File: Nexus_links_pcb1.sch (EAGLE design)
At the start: 41 parts, among them IC1 TL074D, IC4 TL074D, J1 PJ301_THONKICONN6, J10 PJ301_THONKICONN6, J11 PJ301_THONKICONN6, J12 PJ301_THONKICONN6, J2 PJ301_THONKICONN6, J3 PJ301_THONKICONN6, J4 PJ301_THONKICONN6, J5 PJ301_THONKICONN6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

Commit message: updated in december
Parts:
- C1, C2: value 4.7u -> 10u; RSPARTNUMBER (none) -> 568-711
- C3: RSPARTNUMBER (none) -> 264-4416
- C9: RSPARTNUMBER (none) -> 601-0198
- D1, D2: RSPARTNUMBER (none) -> 708-2197
- LED1, LED3: RSPARTNUMBER (none) -> 228-5663

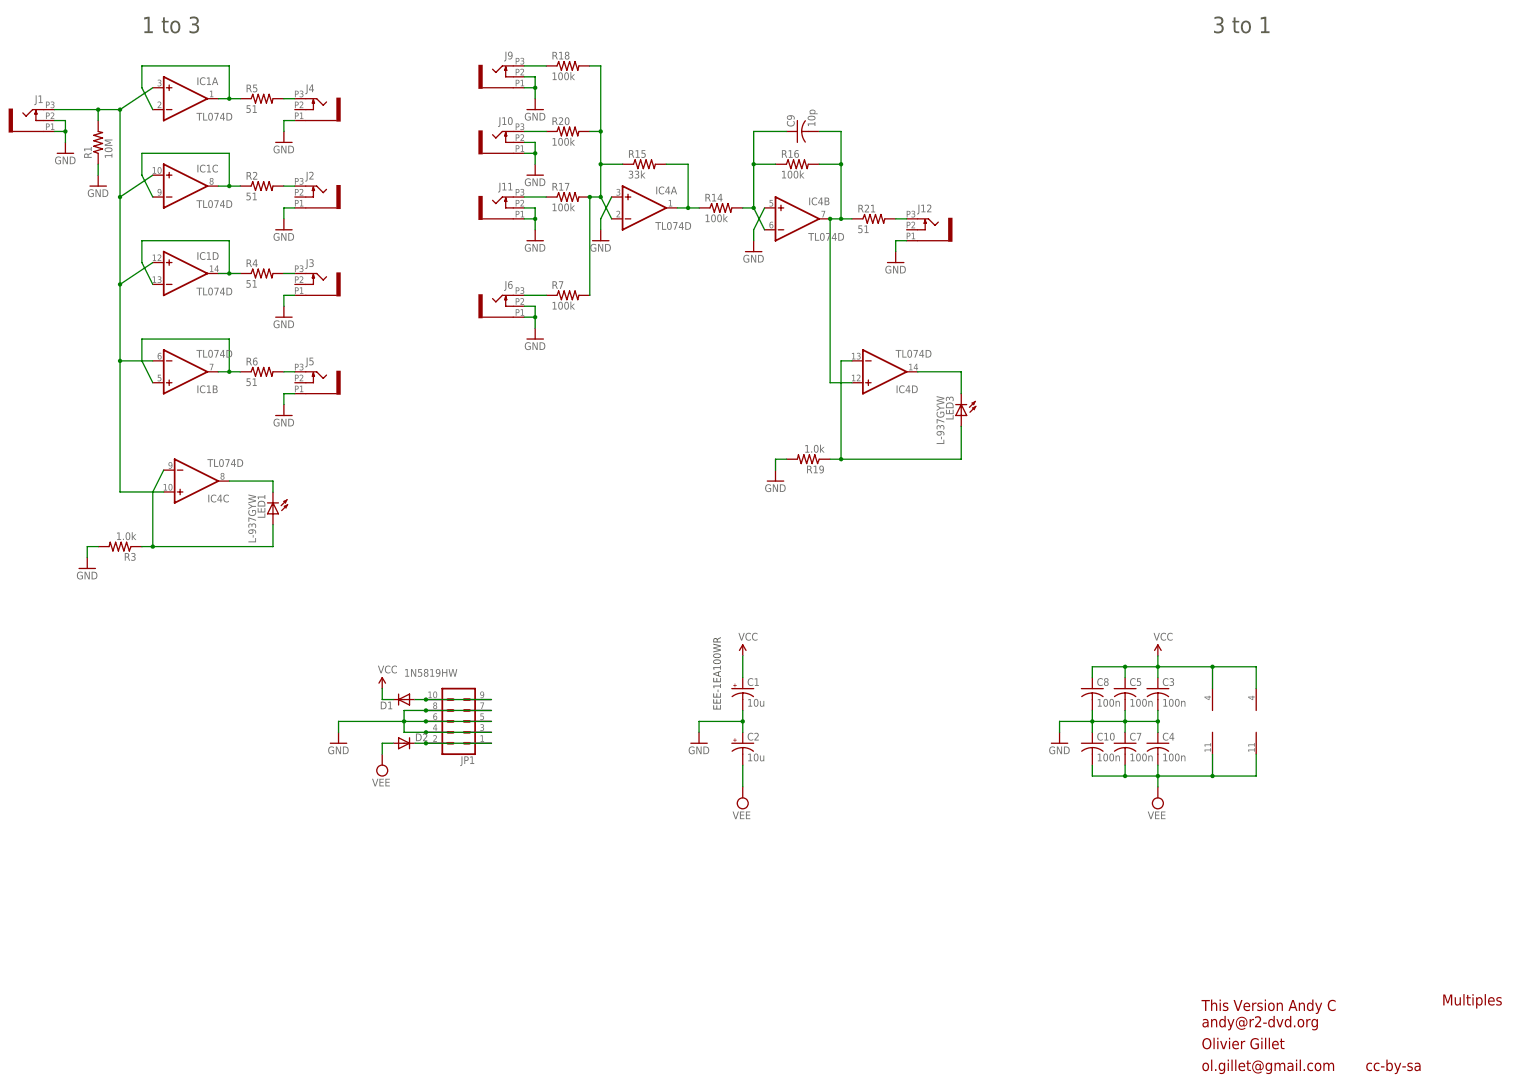
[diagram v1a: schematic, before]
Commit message: updated values to precission adder
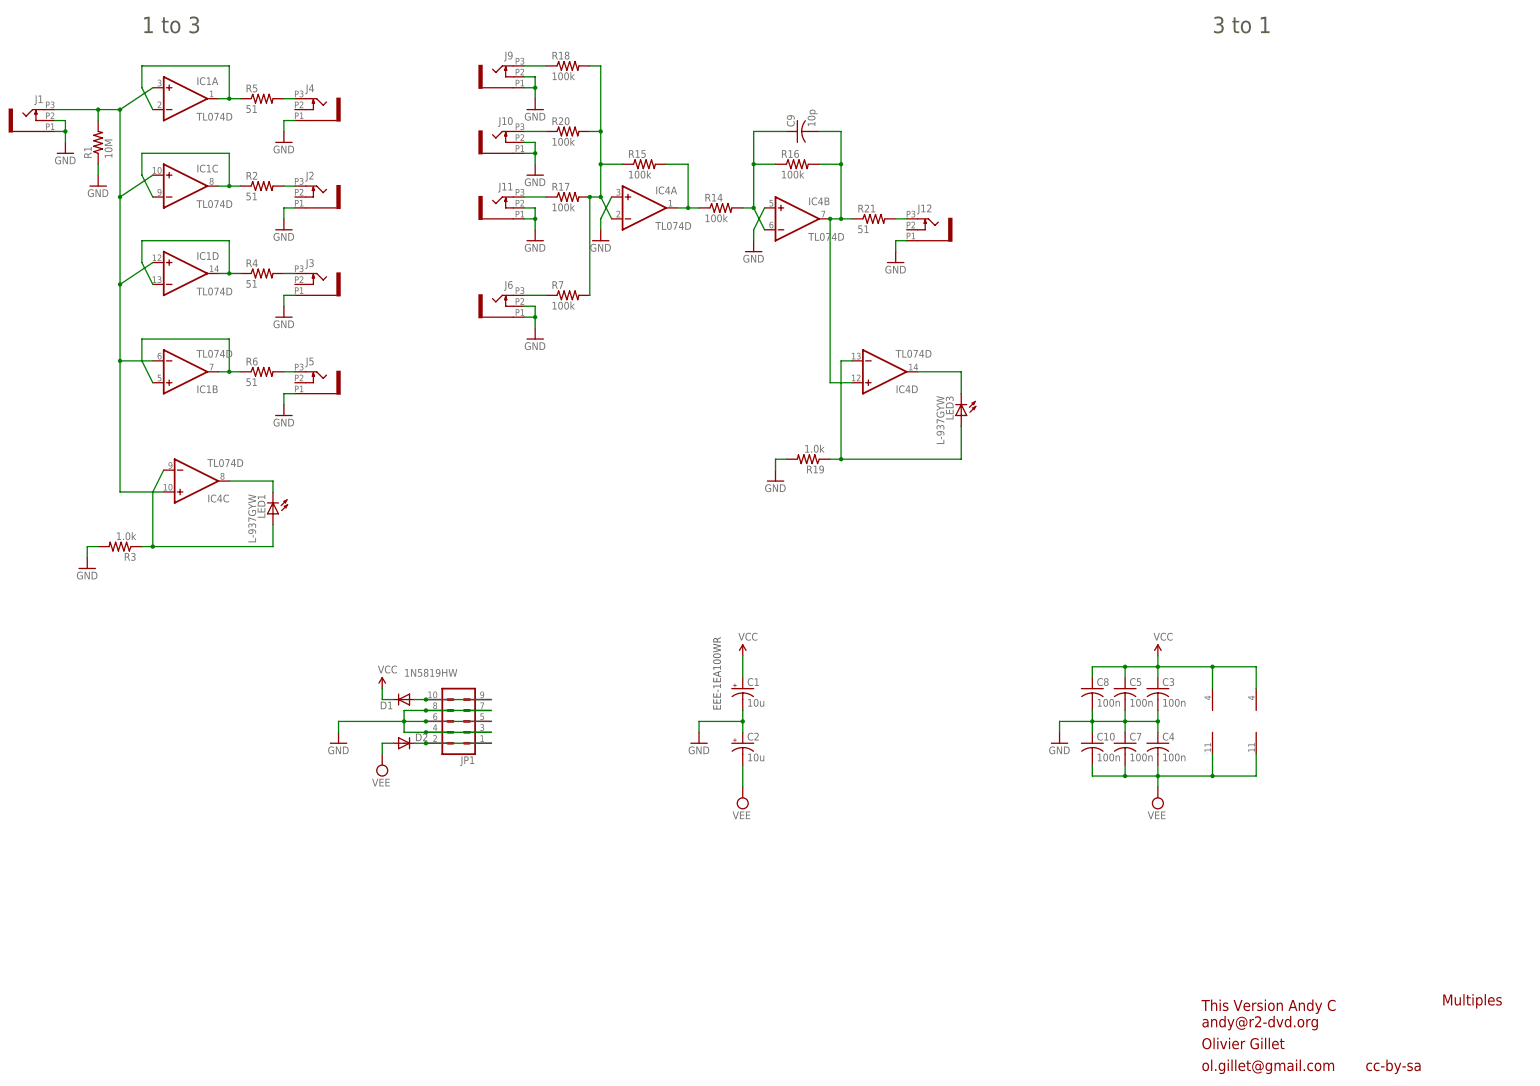
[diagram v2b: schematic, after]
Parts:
- R15: value 33k -> 100k
